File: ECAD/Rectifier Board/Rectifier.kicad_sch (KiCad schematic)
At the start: 26 parts, among them J1 MAINS, Q1 IXFH48N60X3, U2 IR1153S

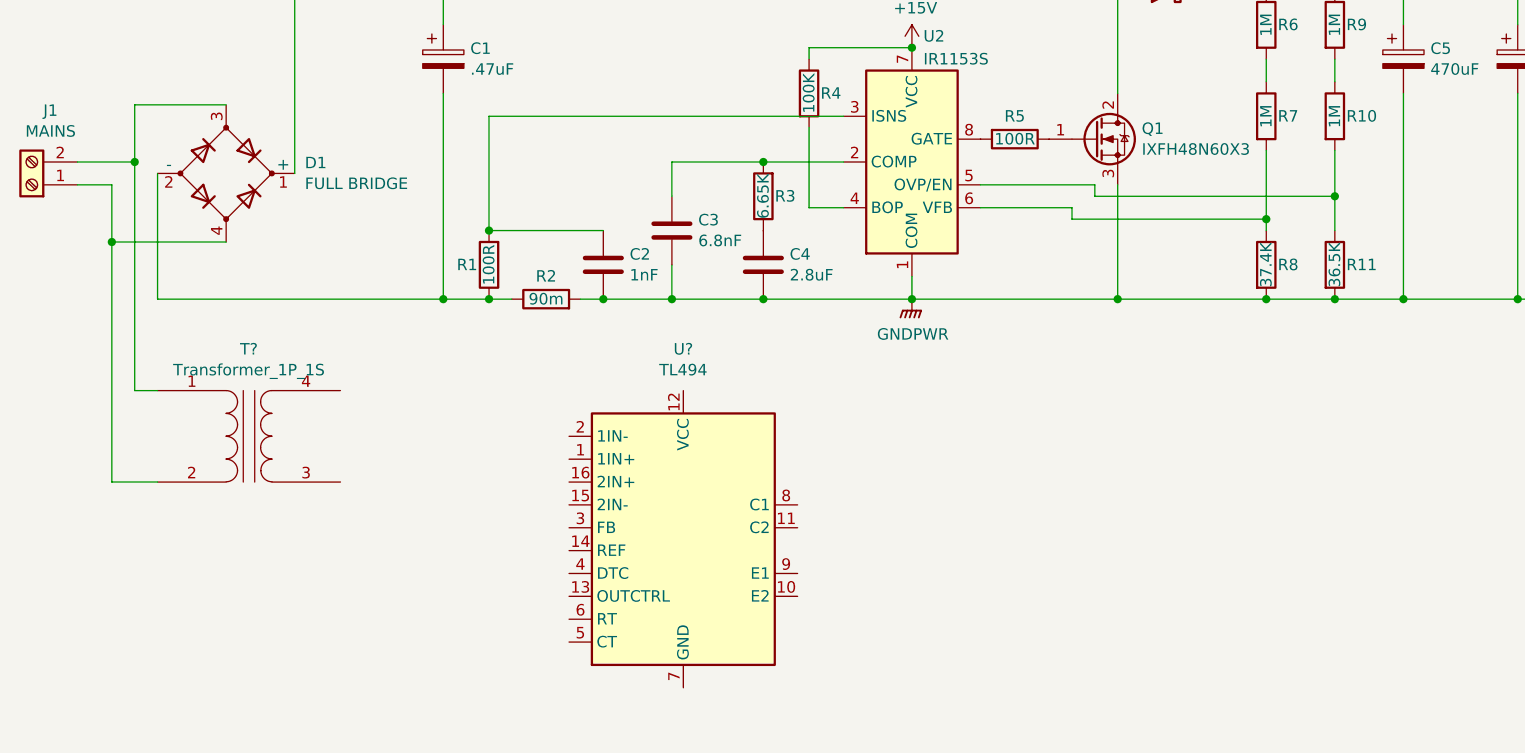
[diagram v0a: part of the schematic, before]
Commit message: Update Rectifier.kicad_sch
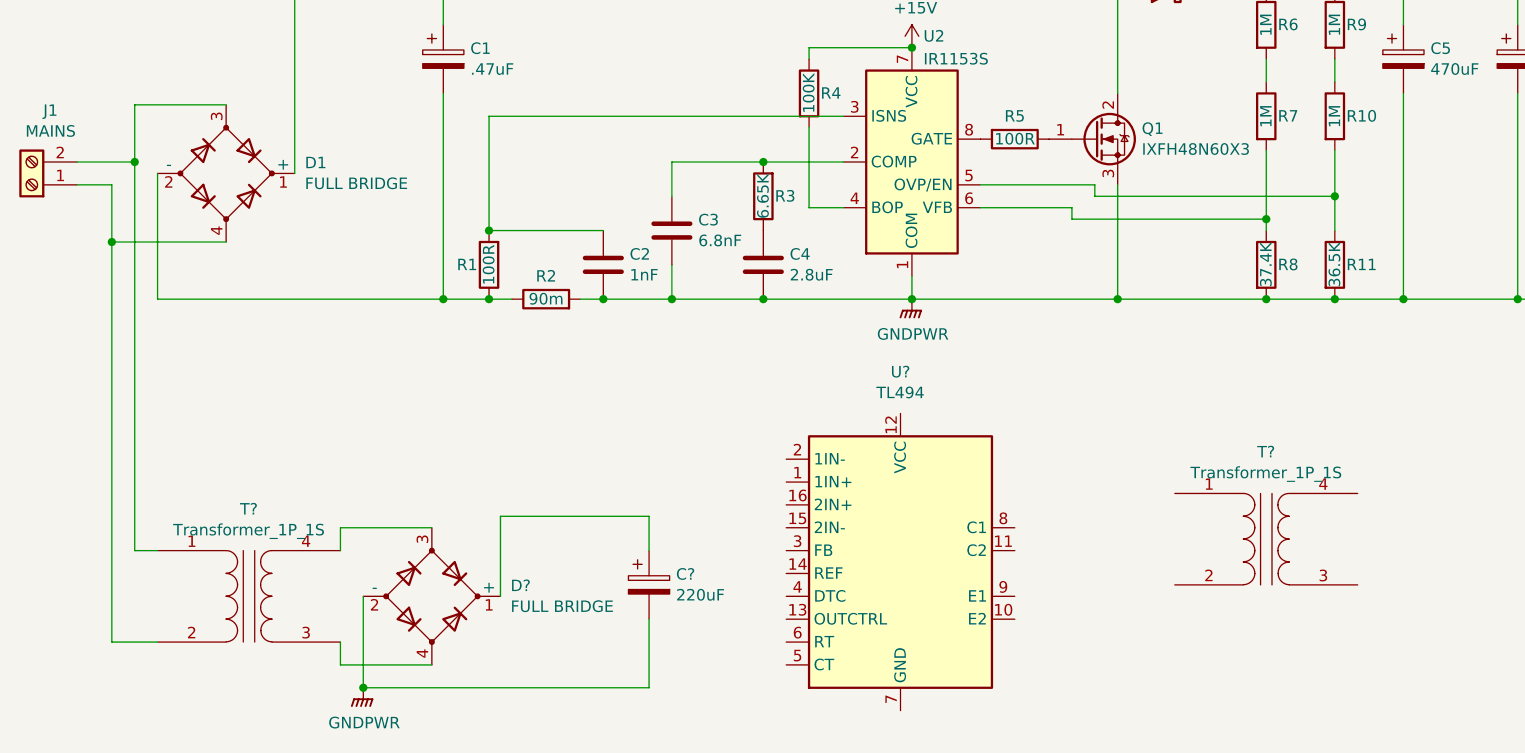
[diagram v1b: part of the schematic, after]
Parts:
- added C?: 220uF, symbol Device:CP
- added D?: FULL BRIDGE, symbol Device:D_Bridge_+-AA
- added T?: Transformer_1P_1S, symbol Device:Transformer_1P_1S
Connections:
- net GNDPWR: now also C?.2, D?.2 (-)
- net at T?.3 (SA): now also D?.4
- net at T?.4 (SB): now also D?.3
- new net: C?.1, D?.1 (+)
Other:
- moved on the sheet: T?, U?
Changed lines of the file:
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@@
 (kicad_sch (version 20211123) (generator eeschema)
-  (paper "A4")
+  (paper "USLegal")
   (junction (at 156.21 22.86) (diameter 0) (color 0 0 0 0)
   )
@@
   (junction (at 184.15 57.15) (diameter 0) (color 0 0 0 0)
   )
+  (junction (at 55.88 100.33) (diameter 0) (color 0 0 0 0)
+  )
   (junction (at 116.84 57.15) (diameter 0) (color 0 0 0 0)
   )
@@
     (stroke (width 0) (type default) (color 0 0 0 0))
   )
+  (wire (pts (xy 53.34 95.25) (xy 53.34 97.79))
+    (stroke (width 0) (type default) (color 0 0 0 0))
+  )
+  (wire (pts (xy 53.34 97.79) (xy 63.5 97.79))
+    (stroke (width 0) (type default) (color 0 0 0 0))
+  )
   (wire (pts (xy 116.84 29.21) (xy 105.41 29.21))
     (stroke (width 0) (type default) (color 0 0 0 0))
@@
     (stroke (width 0) (type default) (color 0 0 0 0))
   )
-  (wire (pts (xy 30.48 67.31) (xy 33.02 67.31))
+  (wire (pts (xy 30.48 85.09) (xy 33.02 85.09))
     (stroke (width 0) (type default) (color 0 0 0 0))
   )
@@
     (stroke (width 0) (type default) (color 0 0 0 0))
   )
+  (wire (pts (xy 87.63 100.33) (xy 87.63 92.71))
+    (stroke (width 0) (type default) (color 0 0 0 0))
+  )
   (wire (pts (xy 105.41 38.1) (xy 105.41 46.99))
     (stroke (width 0) (type default) (color 0 0 0 0))
@@
     (stroke (width 0) (type default) (color 0 0 0 0))
   )
+  (wire (pts (xy 87.63 85.09) (xy 87.63 81.28))
+    (stroke (width 0) (type default) (color 0 0 0 0))
+  )
   (wire (pts (xy 139.7 57.15) (xy 156.21 57.15))
     (stroke (width 0) (type default) (color 0 0 0 0))
@@
     (stroke (width 0) (type default) (color 0 0 0 0))
   )
-  (wire (pts (xy 27.94 77.47) (xy 27.94 50.8))
+  (wire (pts (xy 27.94 50.8) (xy 27.94 95.25))
     (stroke (width 0) (type default) (color 0 0 0 0))
   )
@@
     (stroke (width 0) (type default) (color 0 0 0 0))
   )
-  (wire (pts (xy 33.02 77.47) (xy 27.94 77.47))
+  (wire (pts (xy 33.02 95.25) (xy 27.94 95.25))
     (stroke (width 0) (type default) (color 0 0 0 0))
   )
@@
     (stroke (width 0) (type default) (color 0 0 0 0))
   )
+  (wire (pts (xy 71.12 81.28) (xy 87.63 81.28))
+    (stroke (width 0) (type default) (color 0 0 0 0))
+  )
   (wire (pts (xy 196.85 34.29) (xy 196.85 57.15))
     (stroke (width 0) (type default) (color 0 0 0 0))
@@
     (stroke (width 0) (type default) (color 0 0 0 0))
   )
+  (wire (pts (xy 55.88 90.17) (xy 55.88 100.33))
+    (stroke (width 0) (type default) (color 0 0 0 0))
+  )
   (wire (pts (xy 90.17 41.91) (xy 100.33 41.91))
     (stroke (width 0) (type default) (color 0 0 0 0))
@@
     (stroke (width 0) (type default) (color 0 0 0 0))
   )
-  (wire (pts (xy 30.48 41.91) (xy 30.48 67.31))
+  (wire (pts (xy 30.48 41.91) (xy 30.48 85.09))
     (stroke (width 0) (type default) (color 0 0 0 0))
   )
@@
     (stroke (width 0) (type default) (color 0 0 0 0))
   )
+  (wire (pts (xy 53.34 82.55) (xy 53.34 85.09))
+    (stroke (width 0) (type default) (color 0 0 0 0))
+  )
+  (wire (pts (xy 53.34 82.55) (xy 63.5 82.55))
+    (stroke (width 0) (type default) (color 0 0 0 0))
+  )
   (wire (pts (xy 163.83 33.02) (xy 163.83 30.48))
     (stroke (width 0) (type default) (color 0 0 0 0))
@@
     (stroke (width 0) (type default) (color 0 0 0 0))
   )
+  (wire (pts (xy 71.12 90.17) (xy 71.12 81.28))
+    (stroke (width 0) (type default) (color 0 0 0 0))
+  )
   (wire (pts (xy 184.15 34.29) (xy 184.15 57.15))
     (stroke (width 0) (type default) (color 0 0 0 0))
@@
   )
   (wire (pts (xy 137.16 45.72) (xy 163.83 45.72))
+    (stroke (width 0) (type default) (color 0 0 0 0))
+  )
+  (wire (pts (xy 55.88 100.33) (xy 87.63 100.33))
     (stroke (width 0) (type default) (color 0 0 0 0))
   )
@@
     (pin "2")
   )
-  (symbol (lib_id "Regulator_Controller:TL494") (at 91.44 85.09 0) (unit 1)
-    (in_bom yes) (on_board yes)
-    (property "Reference" "U?" (id 0) (at 91.44 62.7126 0))
-    (property "Value" "TL494" (id 1) (at 91.44 65.024 0))
-    (property "Footprint" "" (id 2) (at 91.44 85.09 0)
-      (effects (font (size 1.27 1.27)) hide)
-    )
-    (property "Datasheet" "http://www.ti.com/lit/ds/symlink/tl494.pdf" (id 3) (at 91.44 85.09 0)
+  (symbol (lib_id "Regulator_Controller:TL494") (at 115.57 87.63 0) (unit 1)
+    (in_bom yes) (on_board yes)
+    (property "Reference" "U?" (id 0) (at 115.57 65.2526 0))
+    (property "Value" "TL494" (id 1) (at 115.57 67.564 0))
+    (property "Footprint" "" (id 2) (at 115.57 87.63 0)
+      (effects (font (size 1.27 1.27)) hide)
+    )
+    (property "Datasheet" "http://www.ti.com/lit/ds/symlink/tl494.pdf" (id 3) (at 115.57 87.63 0)
       (effects (font (size 1.27 1.27)) hide)
     )
@@
     (pin "2")
   )
-  (symbol (lib_id "Device:Transformer_1P_1S") (at 43.18 72.39 0) (unit 1)
-    (in_bom yes) (on_board yes)
-    (property "Reference" "T?" (id 0) (at 43.18 62.7126 0))
-    (property "Value" "Transformer_1P_1S" (id 1) (at 43.18 65.024 0))
-    (property "Footprint" "" (id 2) (at 43.18 72.39 0)
-      (effects (font (size 1.27 1.27)) hide)
-    )
-    (property "Datasheet" "~" (id 3) (at 43.18 72.39 0)
+  (symbol (lib_id "Device:Transformer_1P_1S") (at 43.18 90.17 0) (unit 1)
+    (in_bom yes) (on_board yes)
+    (property "Reference" "T?" (id 0) (at 43.18 80.4926 0))
+    (property "Value" "Transformer_1P_1S" (id 1) (at 43.18 82.804 0))
+    (property "Footprint" "" (id 2) (at 43.18 90.17 0)
+      (effects (font (size 1.27 1.27)) hide)
+    )
+    (property "Datasheet" "~" (id 3) (at 43.18 90.17 0)
       (effects (font (size 1.27 1.27)) hide)
     )
@@
     (pin "3")
     (pin "4")
+  )
+  (symbol (lib_id "Device:Transformer_1P_1S") (at 156.21 83.82 0) (unit 1)
+    (in_bom yes) (on_board yes)
+    (property "Reference" "T?" (id 0) (at 156.21 74.1426 0))
+    (property "Value" "Transformer_1P_1S" (id 1) (at 156.21 76.454 0))
+    (property "Footprint" "" (id 2) (at 156.21 83.82 0)
+      (effects (font (size 1.27 1.27)) hide)
+    )
+    (property "Datasheet" "~" (id 3) (at 156.21 83.82 0)
+      (effects (font (size 1.27 1.27)) hide)
+    )
+    (pin "1")
+    (pin "2")
+    (pin "3")
+    (pin "4")
+  )
+  (symbol (lib_id "power:GNDPWR") (at 55.88 100.33 0) (unit 1)
+    (in_bom yes) (on_board yes)
+    (property "Reference" "#PWR?" (id 0) (at 55.88 105.41 0)
+      (effects (font (size 1.27 1.27)) hide)
+    )
+    (property "Value" "GNDPWR" (id 1) (at 55.9816 104.2416 0))
+    (property "Footprint" "" (id 2) (at 55.88 101.6 0)
+      (effects (font (size 1.27 1.27)) hide)
+    )
+    (property "Datasheet" "" (id 3) (at 55.88 101.6 0)
+      (effects (font (size 1.27 1.27)) hide)
+    )
+    (pin "1")
+  )
+  (symbol (lib_id "Device:D_Bridge_+-AA") (at 63.5 90.17 0) (unit 1)
+    (in_bom yes) (on_board yes)
+    (property "Reference" "D?" (id 0) (at 72.2376 89.0016 0)
+      (effects (font (size 1.27 1.27)) (justify left))
+    )
+    (property "Value" "FULL BRIDGE" (id 1) (at 72.2376 91.313 0)
+      (effects (font (size 1.27 1.27)) (justify left))
+    )
+    (property "Footprint" "" (id 2) (at 63.5 90.17 0)
+      (effects (font (size 1.27 1.27)) hide)
+    )
+    (property "Datasheet" "~" (id 3) (at 63.5 90.17 0)
+      (effects (font (size 1.27 1.27)) hide)
+    )
+    (pin "1")
+    (pin "2")
+    (pin "3")
+    (pin "4")
+  )
+  (symbol (lib_id "Device:CP") (at 87.63 88.9 0) (unit 1)
+    (in_bom yes) (on_board yes)
+    (property "Reference" "C?" (id 0) (at 90.6272 87.7316 0)
+      (effects (font (size 1.27 1.27)) (justify left))
+    )
+    (property "Value" "220uF" (id 1) (at 90.6272 90.043 0)
+      (effects (font (size 1.27 1.27)) (justify left))
+    )
+    (property "Footprint" "" (id 2) (at 88.5952 92.71 0)
+      (effects (font (size 1.27 1.27)) hide)
+    )
+    (property "Datasheet" "~" (id 3) (at 87.63 88.9 0)
+      (effects (font (size 1.27 1.27)) hide)
+    )
+    (pin "1")
+    (pin "2")
   )
   (sheet_instances
@@
       (reference "#PWR03") (unit 1) (value "GNDPWR") (footprint "")
     )
+    (path "/434de308-3c0f-471e-b2ea-4b1db61e07dc"
+      (reference "#PWR?") (unit 1) (value "GNDPWR") (footprint "")
+    )
     (path "/00000000-0000-0000-0000-0000621098c4"
       (reference "C1") (unit 1) (value ".47uF") (footprint "")
@@
       (reference "C7") (unit 1) (value "470uF") (footprint "")
     )
+    (path "/5a1155ab-3629-4b3a-b807-e67c6f1db6ed"
+      (reference "C?") (unit 1) (value "220uF") (footprint "")
+    )
     (path "/00000000-0000-0000-0000-000062057afd"
       (reference "D1") (unit 1) (value "FULL BRIDGE") (footprint "")
@@
       (reference "D2") (unit 1) (value "D_Schottky") (footprint "")
     )
+    (path "/49265804-0096-4217-9537-f218fbd69c52"
+      (reference "D?") (unit 1) (value "FULL BRIDGE") (footprint "")
+    )
     (path "/00000000-0000-0000-0000-000062058fc8"
       (reference "J1") (unit 1) (value "MAINS") (footprint "")
@@
       (reference "T?") (unit 1) (value "Transformer_1P_1S") (footprint "")
     )
+    (path "/2556c191-788e-4d61-8c3b-05091b953499"
+      (reference "T?") (unit 1) (value "Transformer_1P_1S") (footprint "")
+    )

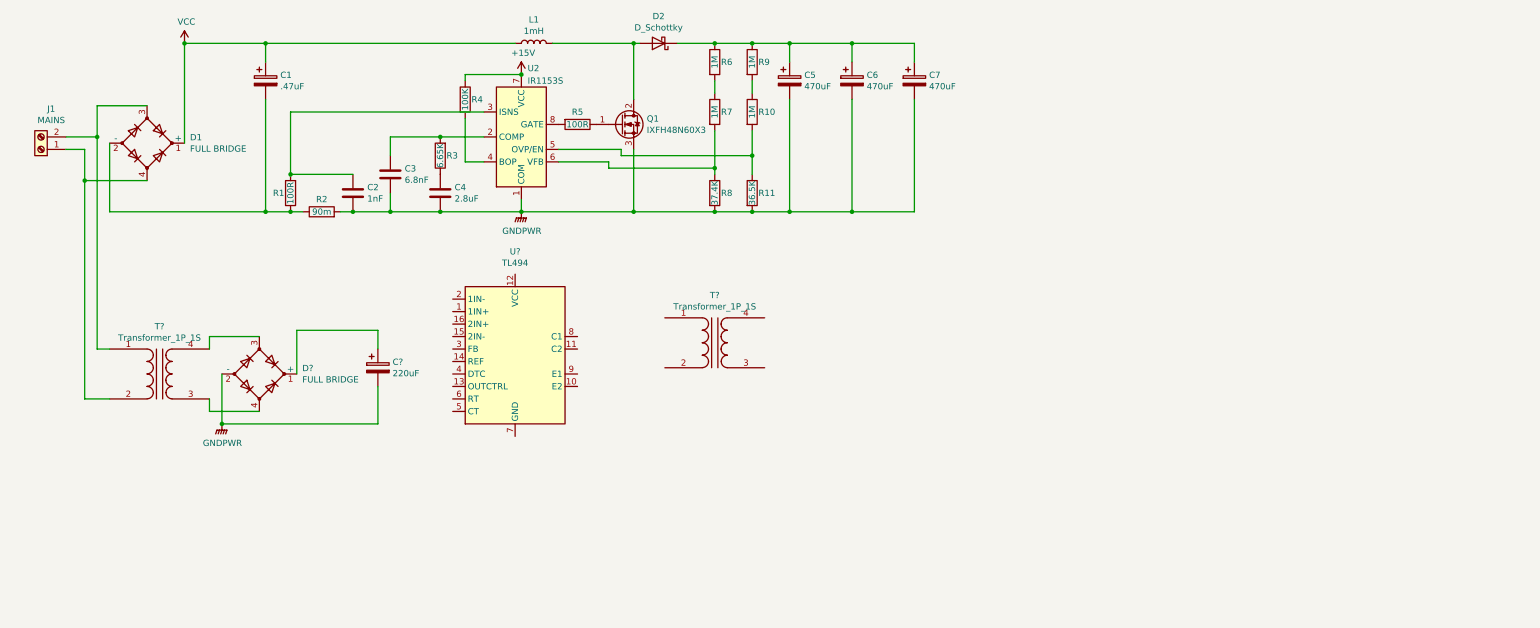
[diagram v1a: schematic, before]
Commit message: separate control from power
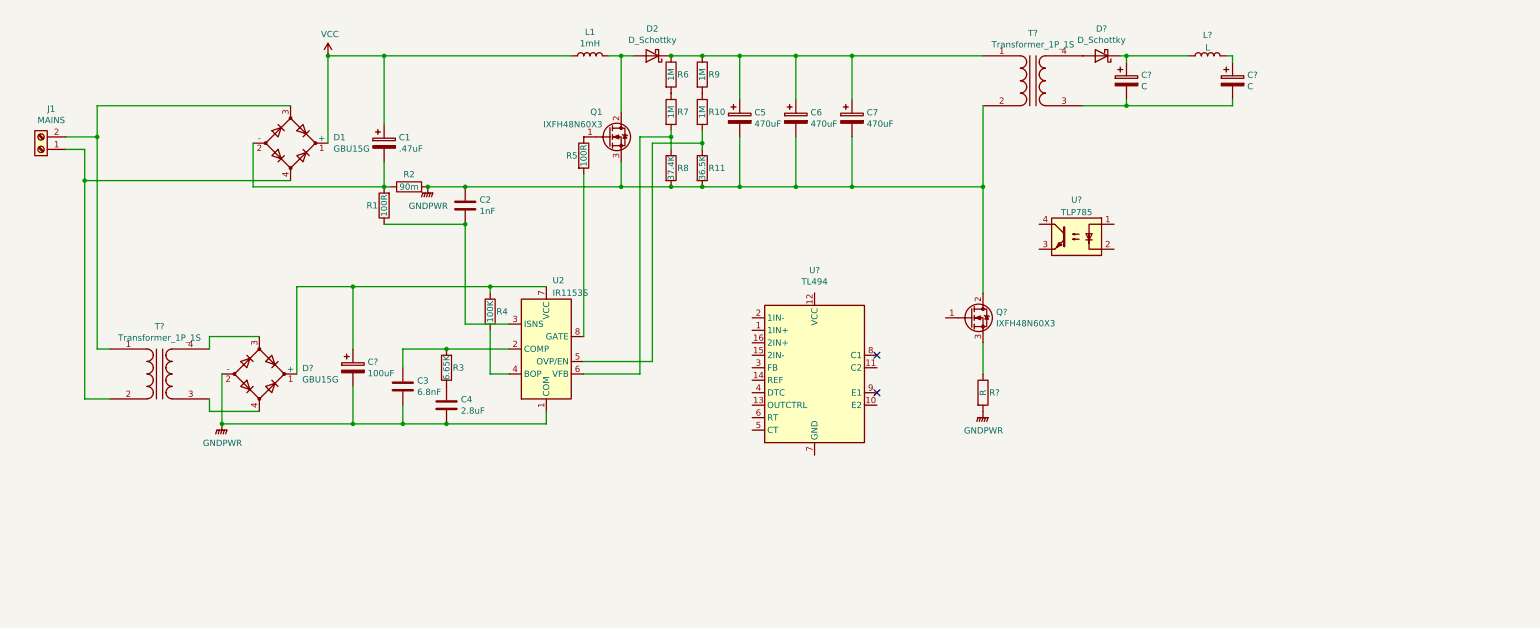
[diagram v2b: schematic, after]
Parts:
- added C? (x2): C, symbol Device:CP
- added D?: D_Schottky, symbol Device:D_Schottky
- added L?: L, symbol Device:L
- added Q?: IXFH48N60X3, Package_TO_SOT_THT:TO-247-3_Vertical, symbol Transistor_FET:C3M0065090D
- added R?: R, symbol Device:R
- added U?: TLP785, Package_DIP:DIP-4_W7.62mm, symbol Isolator:TLP785
- C?: value 220uF -> 100uF
- D1, D?: value FULL BRIDGE -> GBU15G
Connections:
- net +15V is gone; now on an unnamed net: R4.1, U2.7 (VCC)
- net GNDPWR: now also C2.1, T?.2 (AB), Q?.2 (D), R?.2; no longer C2.2
- net at C1.2, D1.2 (-), R2.1: now also R1.2; no longer R1.1
- net at C5.1, C6.1, C7.1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: now also T?.1 (AA)
- net at T?.3 (SA): now also C?.2, C?.2
- net at T?.4 (SB): now also D?.2 (A)
- new net: C2.2, R1.1, U2.3 (ISNS)
- new net: Q?.3 (S), R?.1
- new net: C?.1, D?.1 (K), L?.1
- new net: C?.1, L?.2
- no-connect marks 0 -> 2
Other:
- moved on the sheet: C1, C2, C3, C4, C5, C6, C7, C?, D1, D2, L1, Q1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

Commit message: Place all components, divide sch
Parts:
- removed R?: R, symbol Device:R
- added C? (x5): C, symbol Device:C
- added C?: 1uF, symbol Device:C
- added C?: 22uF, symbol Device:C
- added D?: D, symbol Device:D
- added D?: 1N4148, symbol Device:D
- added D?: 15V, symbol Device:D_Zener
- added J?: DC OUT, symbol Connector:Screw_Terminal_01x02
- added Q? (x2): 2N3019, symbol Device:Q_NPN_EBC
- added Q?: 2N2905, symbol Device:Q_PNP_BCE
- added R? (x16): R, symbol Device:R
- added R?: 10K, symbol Device:R_Trim
- added U? (x3): LM393, symbol Comparator:LM393
- added U?: TL431DBV, Package_TO_SOT_SMD:SOT-23-5, symbol Reference_Voltage:TL431DBV
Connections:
- net GNDPWR: now also U?.13 (OUTCTRL), U?.16 (2IN+), U?.7 (GND), C?.2, C?.2, C?.2, D?.2 (A), Q?.1 (E), Q?.2 (C), R?.2, R?.2, R?.2, R?.2, R?.2, R?.2, U?.4 (V-), U?.5 (+), U?.6 (_); no longer Q?.2 (D), T?.2 (AB)
- net +15V: now reaches C?.1, D?.1 (+), R4.1, U2.7 (VCC)
- net +15V: now also U?.11 (C2), U?.12 (VCC), U?.4, C?.1, C?.1, Q?.3 (C), U?.8 (V+)
- net at C5.1, C6.1, C7.1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: now also C?.1, R?.1
- net at U?.1 (1IN+): now also U?.3, R?.1
- net at U?.10 (E2): now also Q?.3 (C), R?.1
- net at U?.14 (REF): now also U?.15 (2IN-), C?.1, R?.1, R?.1
- net at U?.2 (1IN-): now also U?.3 (FB)
- net at U?.4 (DTC): now also C?.2, R?.1, R?.2
- net at U?.5 (CT): now also C?.1
- net at U?.6 (RT): now also R?.1
- net GND: now reaches C?.2, C?.2, T?.3 (SA)
- net GND: now also C?.2, J?.1 (Pin_1), R?.2, U?.5 (A)
- net at Q?.1 (G): now also D?.1 (K), D?.1 (K), Q?.3 (E)
- net at Q?.3 (S): now also R?.1, U?.3 (+)
- net at C?.1, D?.1 (K), L?.1: now also R?.2
- net at C?.1, L?.2: now also J?.2 (Pin_2), R?.1
- net at U?.1: now also R?.1, R?.1
- net at U?.2: now also C?.1, C?.1, R?.2, U?.3 (K)
- net VCC renamed VAA
- new net: C?.2, D?.1 (K), R?.2
- new net: D?.2 (A), Q?.2 (D), T?.2 (AB)
- new net: D?.2 (A), Q?.1 (B), R?.1, R?.1
- new net: R?.1, R?.2, U?.2 (-)
- new net: Q?.1 (E), R?.2
- new net: Q?.2 (B), R?.2
- new net: Q?.2 (B), R?.1
- new net: R?.2, U?.1
- new net: R?.1, R?.2, R?.2, U?.4 (REF)
- new net: C?.2, R?.1
- no-connect marks 2 -> 3
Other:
- note added: "15V Control Supply"
- note added: "APFC"
- note added: "APFC Control"
- note added: "Control"
- note added: "Flyback Control"
- note added: "Flyback Power"
- note added: "Isolated Feedback"
- note added: "Isolated Output"
- note added: "Power"
- note added: "Rectifier"
- moved on the sheet: C1, C2, C3, C4, C5, C6, C7, C?, D1, D2, D?, J1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
